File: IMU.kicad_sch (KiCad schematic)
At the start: 19 parts, among them U27 NTS0102_XSON, U28 NTB0102_XSON, U29 ICM-20948

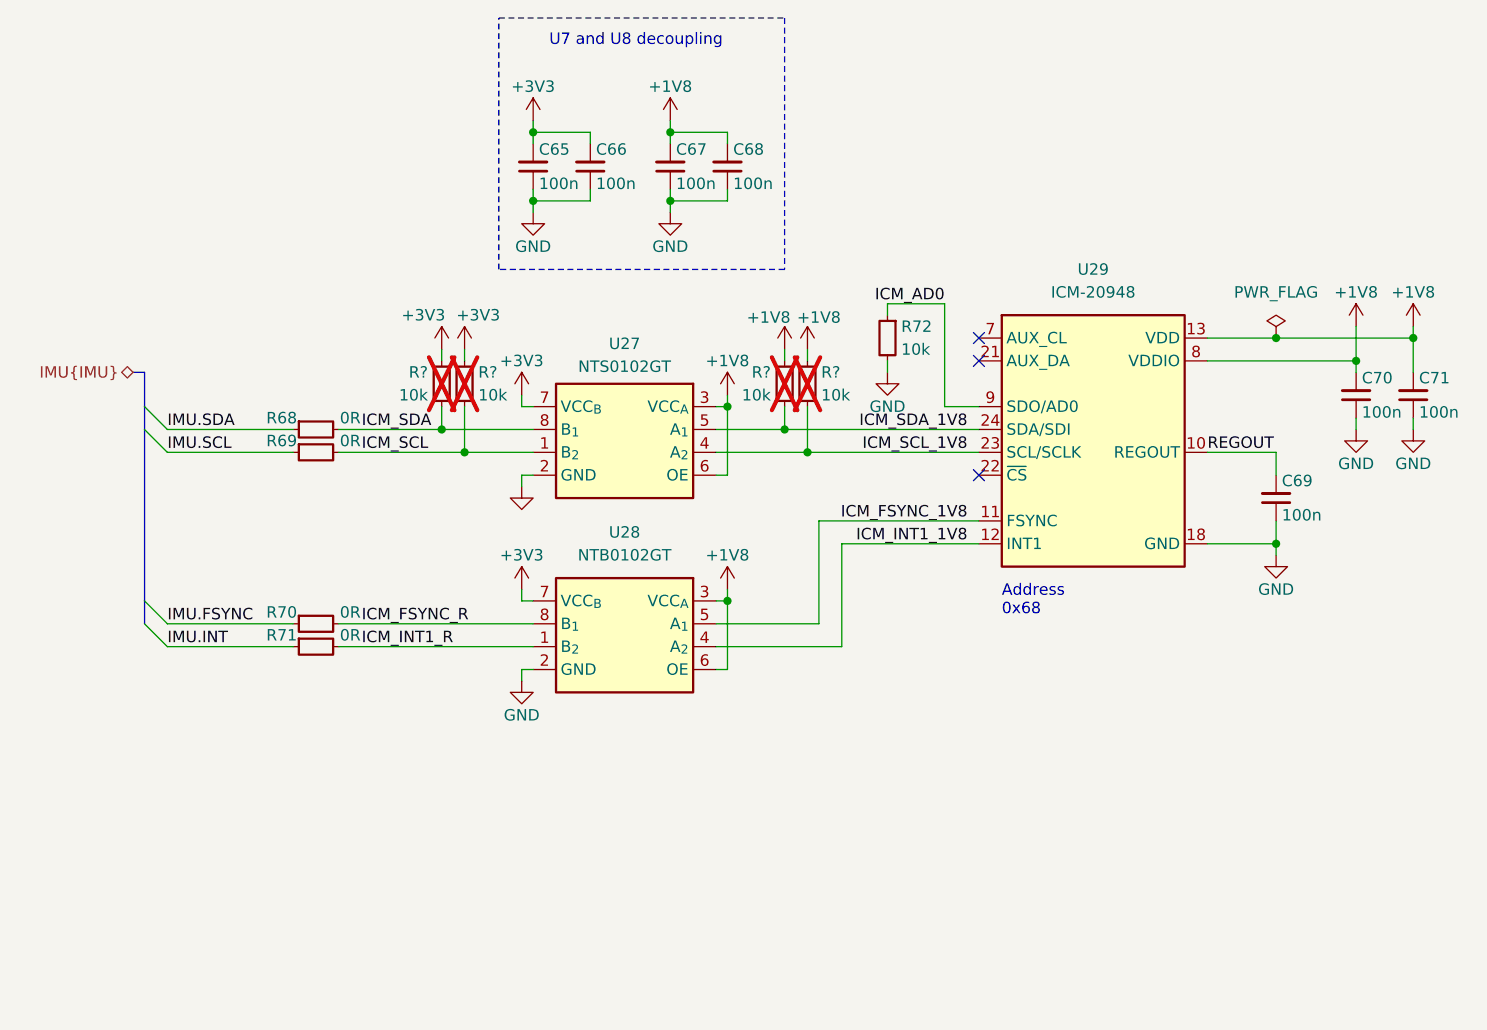
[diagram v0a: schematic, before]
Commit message: [#72133] Sch: Update power section
Signed-off-by: Dawid Lentka <dlentka@antmicro.com>
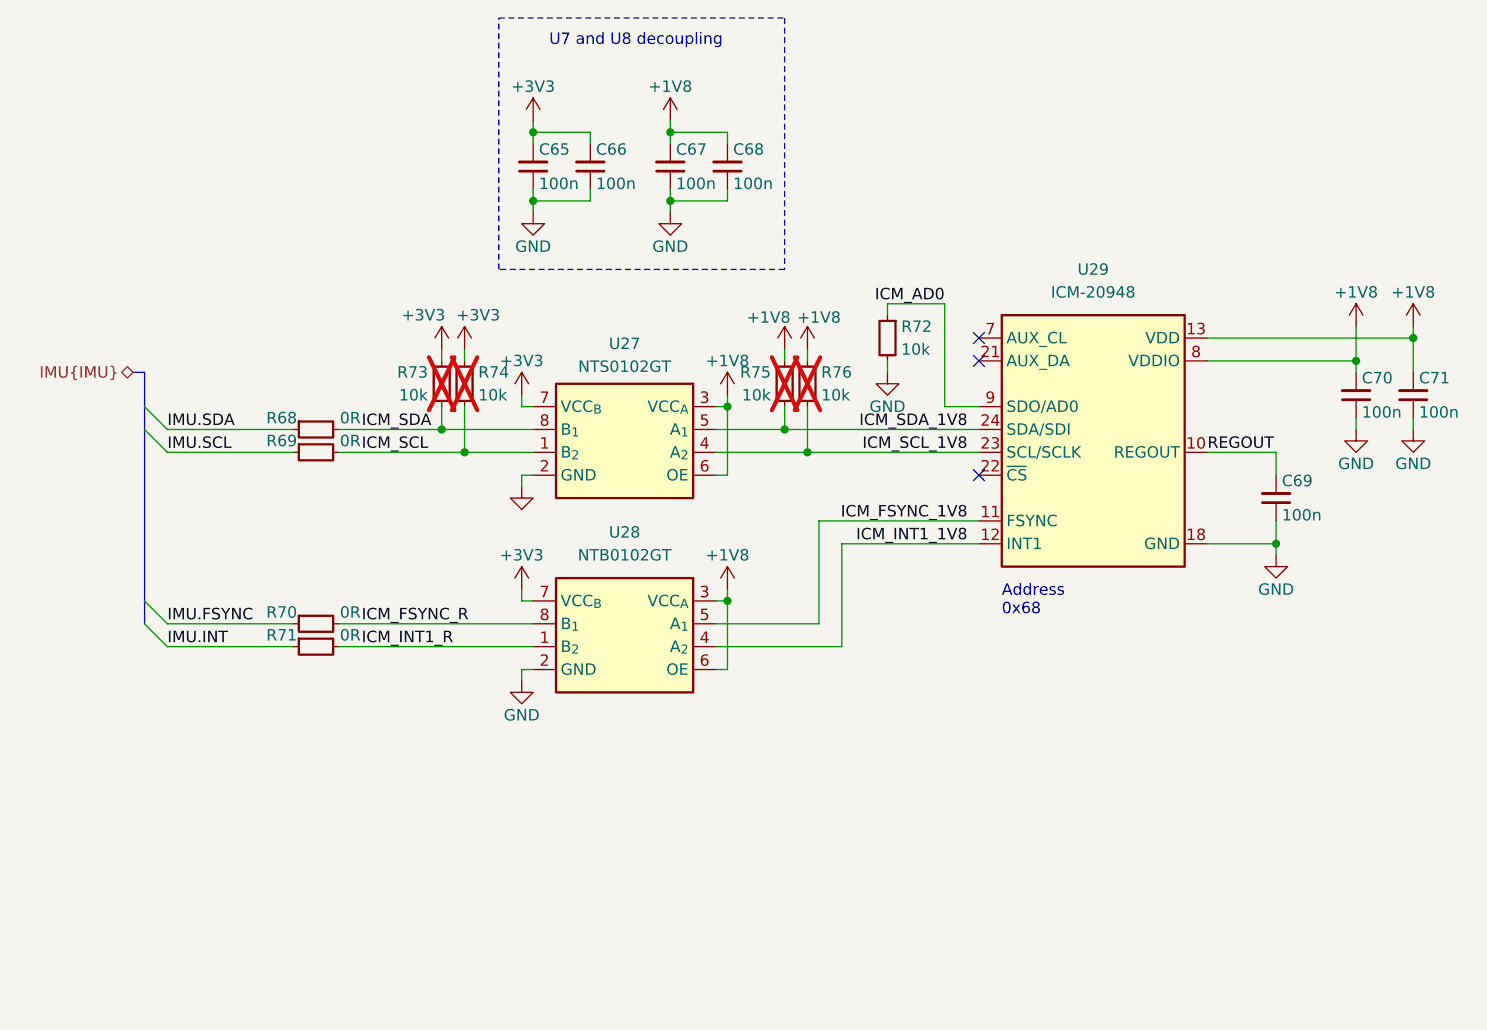
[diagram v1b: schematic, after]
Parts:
- gave numbers to parts that had none: 4
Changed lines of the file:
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@@
 	)
 	(junction
-		(at 209.55 92.71)
-		(diameter 0)
-		(color 0 0 0 0)
-	)
-	(junction
 		(at 224.79 92.71)
 		(diameter 0)
@@
 	(wire
 		(pts
-			(xy 209.55 92.71) (xy 224.79 92.71)
+			(xy 201.93 92.71) (xy 224.79 92.71)
 		)
 		(stroke
@@
 	(wire
 		(pts
-			(xy 201.93 92.71) (xy 209.55 92.71)
-		)
-		(stroke
-			(width 0)
-			(type default)
-		)
-	)
-	(wire
-		(pts
 			(xy 157.48 93.98) (xy 157.48 95.25)
 		)
@@
 	(label "IMU.SDA"
 		(at 86.36 102.87 0)
+		(fields_autoplaced yes)
 		(effects
 			(font
@@
 	(label "IMU.FSYNC"
 		(at 86.36 124.46 0)
+		(fields_autoplaced yes)
 		(effects
 			(font
@@
 	(label "IMU.SCL"
 		(at 86.36 105.41 0)
+		(fields_autoplaced yes)
 		(effects
 			(font
@@
 	(label "IMU.INT"
 		(at 86.36 127 0)
+		(fields_autoplaced yes)
 		(effects
 			(font
@@
 	)
 	(symbol
-		(lib_id "antmicropower:PWR_FLAG")
-		(at 209.55 92.71 0)
-		(unit 1)
-		(exclude_from_sim no)
-		(in_bom yes)
-		(on_board yes)
-		(dnp no)
-		(fields_autoplaced yes)
-		(property "Reference" "#FLG03"
-			(at 209.55 90.805 0)
-			(effects
-				(font
-					(size 1.27 1.27)
-				)
-				(hide yes)
-			)
-		)
-		(property "Value" "PWR_FLAG"
-			(at 209.55 87.63 0)
-			(effects
-				(font
-					(size 1.27 1.27)
-				)
-			)
-		)
-		(property "Footprint" ""
-			(at 209.55 92.71 0)
-			(effects
-				(font
-					(size 1.27 1.27)
-				)
-				(hide yes)
-			)
-		)
-		(property "Datasheet" ""
-			(at 209.55 92.71 0)
-			(effects
-				(font
-					(size 1.27 1.27)
-				)
-				(hide yes)
-			)
-		)
-		(property "Description" ""
-			(at 209.55 92.71 0)
-			(effects
-				(font
-					(size 1.27 1.27)
-				)
-				(hide yes)
-			)
-		)
-		(pin "1"
-		)
-		(instances
-			(project "led-panel"
-				(path "/a86e1cab-ea0a-45e6-9194-d44b0d5c9450/7d74e2d4-6915-4751-a0d0-a23155c065e5"
-					(reference "#FLG03")
-					(unit 1)
-				)
-			)
-		)
-	)
-	(symbol
 		(lib_id "antmicroLogicTranslatorsLevelShifters:NTS0102_XSON")
 		(at 147.32 100.33 0)
@@
 		(on_board yes)
 		(dnp yes)
-		(property "Reference" "R?"
+		(property "Reference" "R75"
 			(at 153.416 96.52 90)
 			(effects
@@
 			(project "led-panel"
 				(path "/a86e1cab-ea0a-45e6-9194-d44b0d5c9450/7d74e2d4-6915-4751-a0d0-a23155c065e5"
-					(reference "R?")
+					(reference "R75")
 					(unit 1)
 				)
@@
 		(on_board yes)
 		(dnp yes)
-		(property "Reference" "R?"
+		(property "Reference" "R76"
 			(at 159.004 96.52 90)
 			(effects
@@
 			(project "led-panel"
 				(path "/a86e1cab-ea0a-45e6-9194-d44b0d5c9450/7d74e2d4-6915-4751-a0d0-a23155c065e5"
-					(reference "R?")
+					(reference "R76")
 					(unit 1)
 				)
@@
 		(on_board yes)
 		(dnp yes)
-		(property "Reference" "R?"
+		(property "Reference" "R74"
 			(at 120.904 96.52 90)
 			(effects
@@
 			(project "led-panel"
 				(path "/a86e1cab-ea0a-45e6-9194-d44b0d5c9450/7d74e2d4-6915-4751-a0d0-a23155c065e5"
-					(reference "R?")
+					(reference "R74")
 					(unit 1)
 				)
@@
 		(on_board yes)
 		(dnp yes)
-		(property "Reference" "R?"
+		(property "Reference" "R73"
 			(at 115.316 96.52 90)
 			(effects
@@
 			(project "led-panel"
 				(path "/a86e1cab-ea0a-45e6-9194-d44b0d5c9450/7d74e2d4-6915-4751-a0d0-a23155c065e5"
-					(reference "R?")
+					(reference "R73")
 					(unit 1)
 				)

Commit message: [#72133] Update supply schematic
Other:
- title: (none) -> LED Panel Board
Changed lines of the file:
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@@
 	(generator_version "8.0")
 	(paper "A4")
+	(title_block
+		(title "LED Panel Board")
+		(date "2025-01-31")
+		(rev "1.0.0")
+	)
 	(bus_alias "IMU"
 		(members "SCL" "SDA" "FSYNC" "INT")

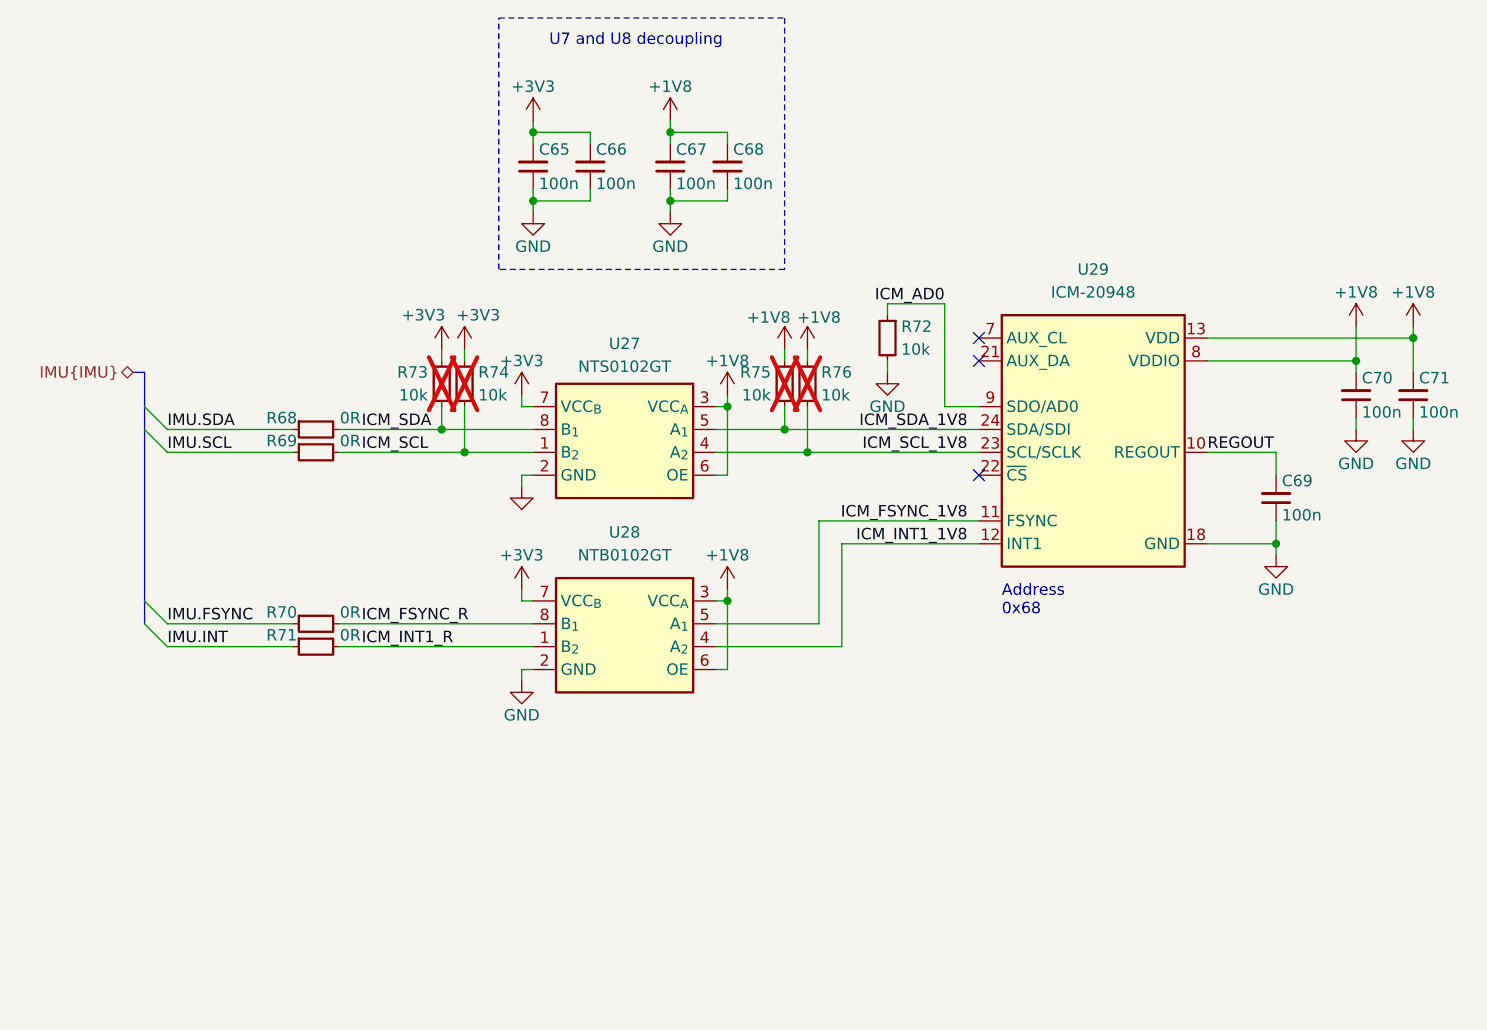
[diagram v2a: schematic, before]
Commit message: [#72133] Add captions to schematic sheets
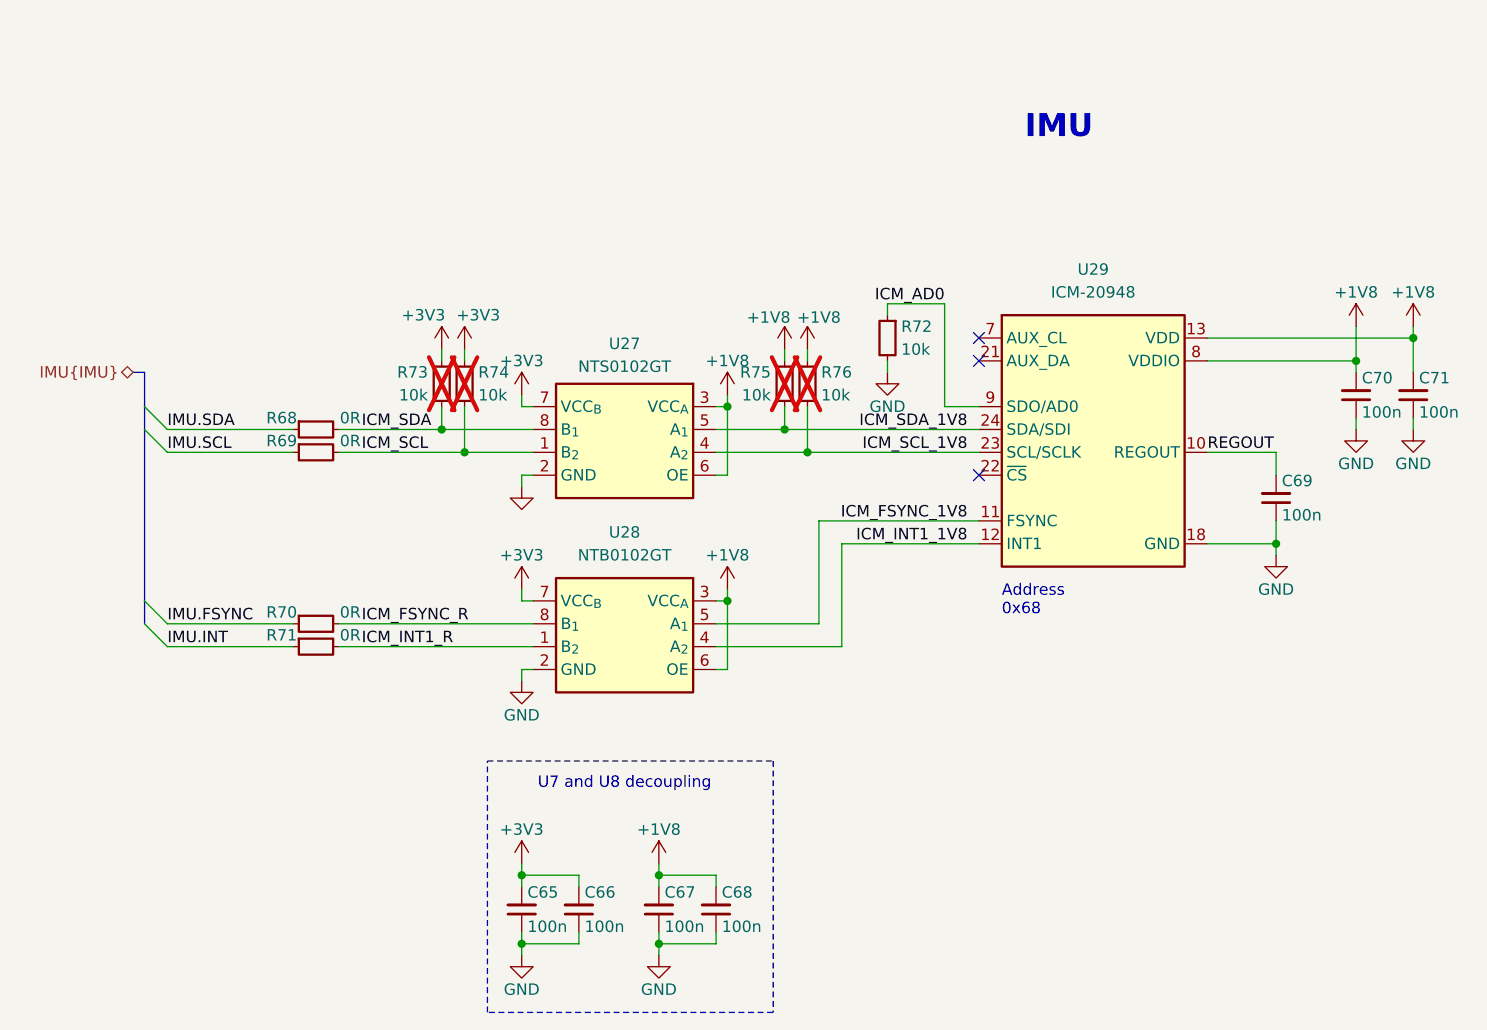
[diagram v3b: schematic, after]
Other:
- note added: "IMU"
- moved on the sheet: C65, C66, C67, C68

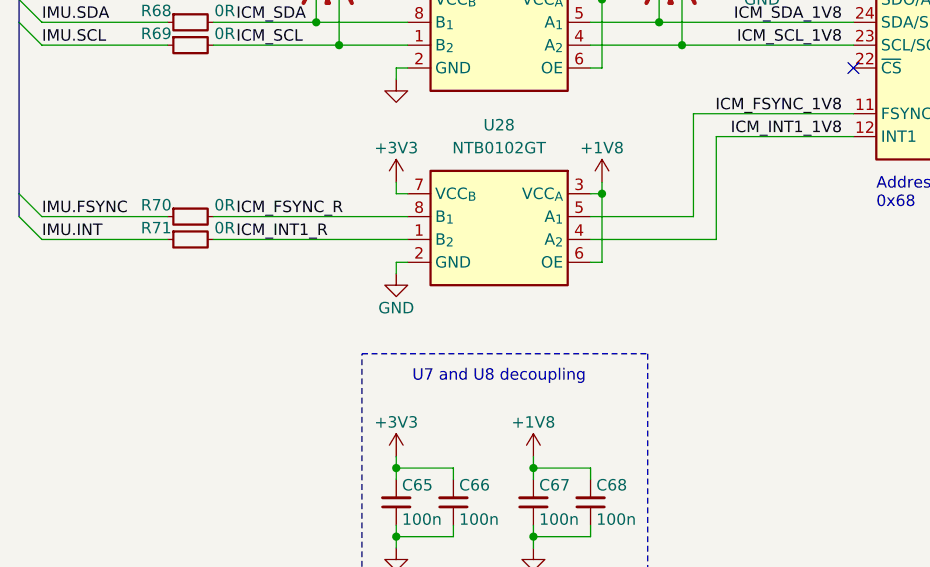
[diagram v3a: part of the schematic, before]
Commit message: [#72447] Add pulldown on IMU.FSYNC
Signed-off-by: Dawid Lentka <dlentka@antmicro.com>
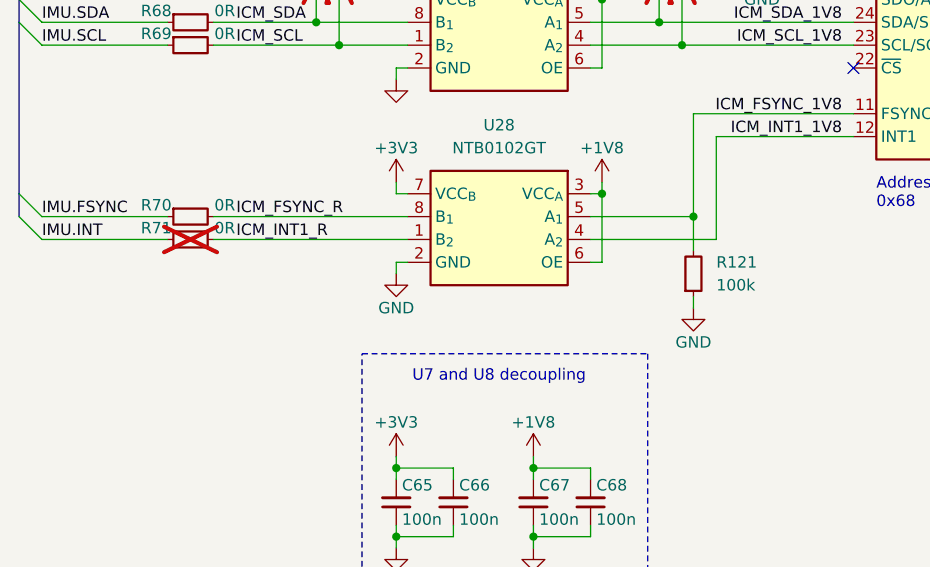
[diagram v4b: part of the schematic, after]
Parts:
- added R121: R_100k_0402, antmicro-footprints:R_0402_1005Metric, symbol antmicroResistors0402:R_100k_0402
- R71: now not fitted
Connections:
- net GND: now also R121.1
- net ICM_FSYNC_1V8: now also R121.2

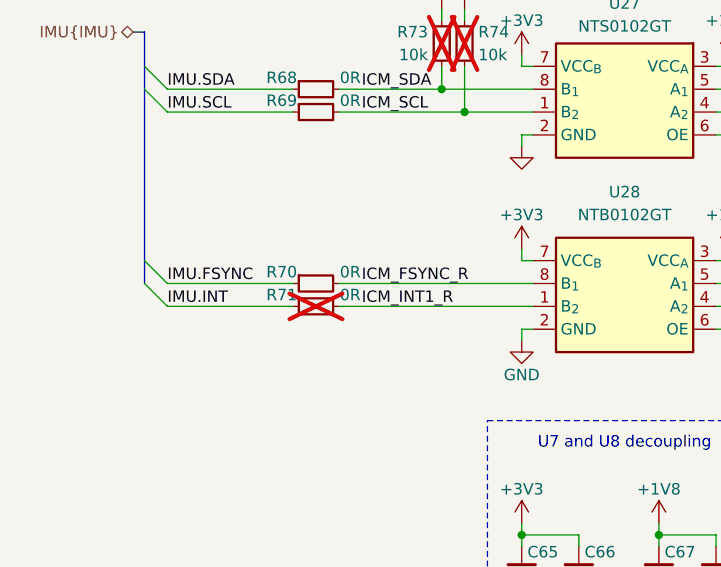
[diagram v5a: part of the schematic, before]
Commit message: [#72447] Update designators
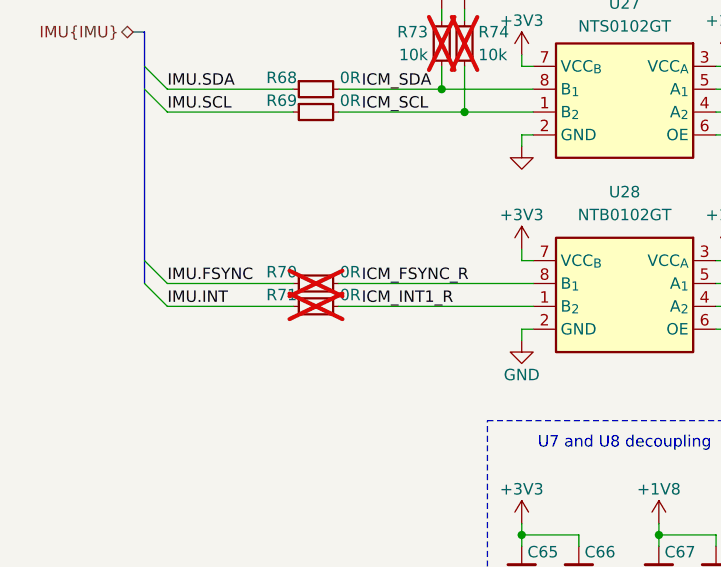
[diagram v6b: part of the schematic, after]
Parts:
- R70: now not fitted; now left out of the parts list
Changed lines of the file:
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@@
 	(title_block
 		(title "LED Panel Board")
-		(date "2025-02-04")
+		(date "2025-01-31")
 		(rev "1.0.0")
 	)
@@
 		(unit 1)
 		(exclude_from_sim no)
-		(in_bom yes)
+		(in_bom no)
 		(on_board yes)
-		(dnp no)
+		(dnp yes)
 		(property "Reference" "R70"
 			(at 99.06 123.19 0)
